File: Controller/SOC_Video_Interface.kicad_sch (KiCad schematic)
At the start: 27 parts, among them J2 HDMI_A_1.4, J55 Conn_01x22_MountingPin, U11 AM6252ASGFHIAMCRQ1, U14 74LVC1G08, U27 TPD12S016RKTR, U7 SII9022

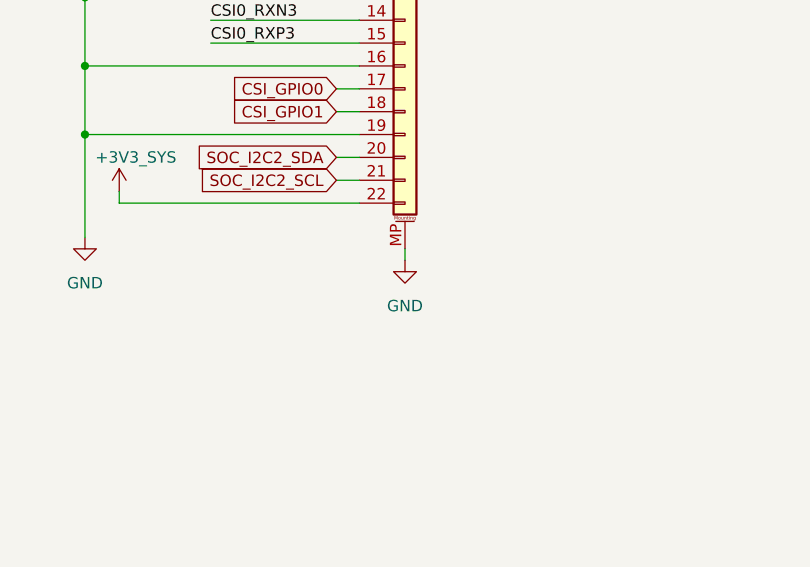
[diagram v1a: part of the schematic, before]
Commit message: DDR_CLK termination
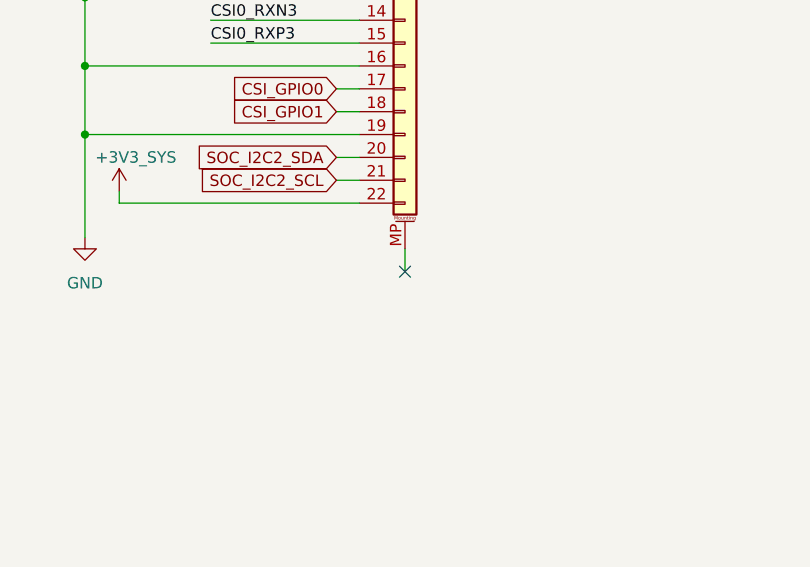
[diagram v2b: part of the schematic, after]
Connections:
- net GND: no longer J55.MP (MountPin)
- no-connect marks 1 -> 2
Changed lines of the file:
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@@
 	)
 	(no_connect
+		(at 274.32 194.31)
+	)
+	(no_connect
 		(at 64.77 134.62)
 	)
@@
 	(wire
 		(pts
-			(xy 274.32 191.77) (xy 274.32 193.04)
-		)
-		(stroke
-			(width 0)
-			(type default)
-		)
-	)
-	(wire
-		(pts
 			(xy 72.39 172.72) (xy 72.39 173.99)
 		)
@@
 	(wire
 		(pts
+			(xy 274.32 194.31) (xy 274.32 191.77)
+		)
+		(stroke
+			(width 0)
+			(type default)
+		)
+	)
+	(wire
+		(pts
 			(xy 156.21 151.13) (xy 143.51 151.13)
 		)
@@
 					(unit 1)
 				)
-			)
-		)
-	)
-	(symbol
-		(lib_id "power:GND")
-		(at 274.32 193.04 0)
-		(unit 1)
-		(body_style 1)
-		(exclude_from_sim no)
-		(in_bom yes)
-		(on_board yes)
-		(in_pos_files yes)
-		(dnp no)
-		(fields_autoplaced yes)
-		(property "Reference" "#PWR0167"
-			(at 274.32 199.39 0)
-			(hide yes)
-			(show_name no)
-			(do_not_autoplace no)
-			(effects
-				(font
-					(size 1.27 1.27)
-				)
-			)
-		)
-		(property "Value" "GND"
-			(at 274.32 198.12 0)
-			(show_name no)
-			(do_not_autoplace no)
-			(effects
-				(font
-					(size 1.27 1.27)
-				)
-			)
-		)
-		(property "Footprint" ""
-			(at 274.32 193.04 0)
-			(hide yes)
-			(show_name no)
-			(do_not_autoplace no)
-			(effects
-				(font
-					(size 1.27 1.27)
-				)
-			)
-		)
-		(property "Datasheet" ""
-			(at 274.32 193.04 0)
-			(hide yes)
-			(show_name no)
-			(do_not_autoplace no)
-			(effects
-				(font
-					(size 1.27 1.27)
-				)
-			)
-		)
-		(property "Description" "Power symbol creates a global label with name \"GND\" , ground"
-			(at 274.32 193.04 0)
-			(hide yes)
-			(show_name no)
-			(do_not_autoplace no)
-			(effects
-				(font
-					(size 1.27 1.27)
-				)
-			)
-		)
-		(pin "1"
-		)
-		(instances
-			(project "Controller"
-				(path "/2c9e7a41-63e4-4339-89dd-991e772f7a19/6314d9d9-bf56-456f-978f-8fa96e5a8ad9"
-					(reference "#PWR0167")
-					(unit 1)
-				)

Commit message: Testpoints + DDR velocity comp
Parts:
- added TP34: TestPoint, TestPoint:TestPoint_Pad_D1.5mm, symbol Connector:TestPoint
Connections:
- net HDMI_RSTn: now also TP34.1
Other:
- note added: "22-Pin 4 Lane CSI-2"
- note removed: "15-Pin 2 Lane CSI-2"
- note removed: "40-Pin LVDS ?? 8 data pairs + 2 clock pairs"
- moved on the sheet: C328, C91, J2, J55, R187, U11A, U27
